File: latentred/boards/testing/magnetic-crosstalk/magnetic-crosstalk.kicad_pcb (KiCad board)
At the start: 4 copper layers, 82.4 x 89 mm, 93 parts, among them J1 STEWART_SS_74500_024, J2 SMA, J3 SMA, J4 SMA, J5 SMA, J6 SMA, J7 SMA, J8 SMA, J9 SMA

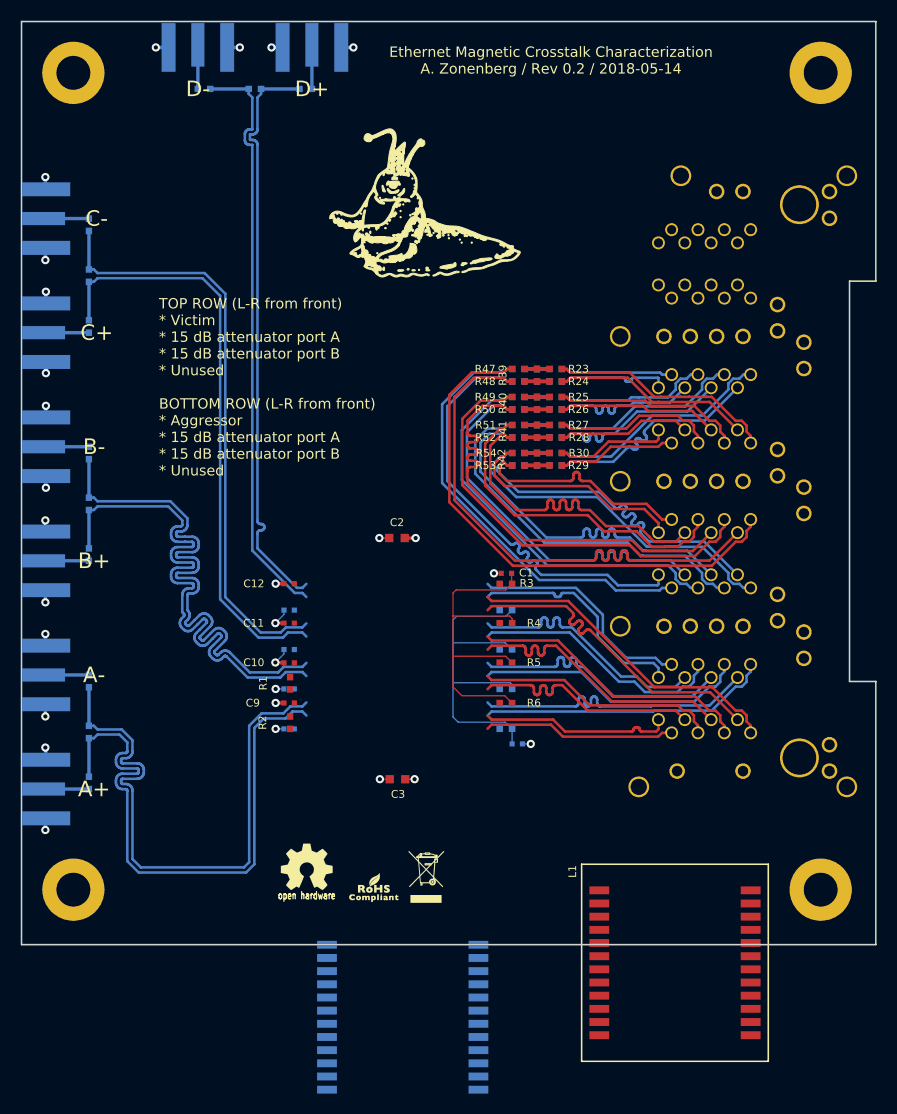
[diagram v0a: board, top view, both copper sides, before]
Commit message: Fixed pinout bugs. v0.2 PCB release.
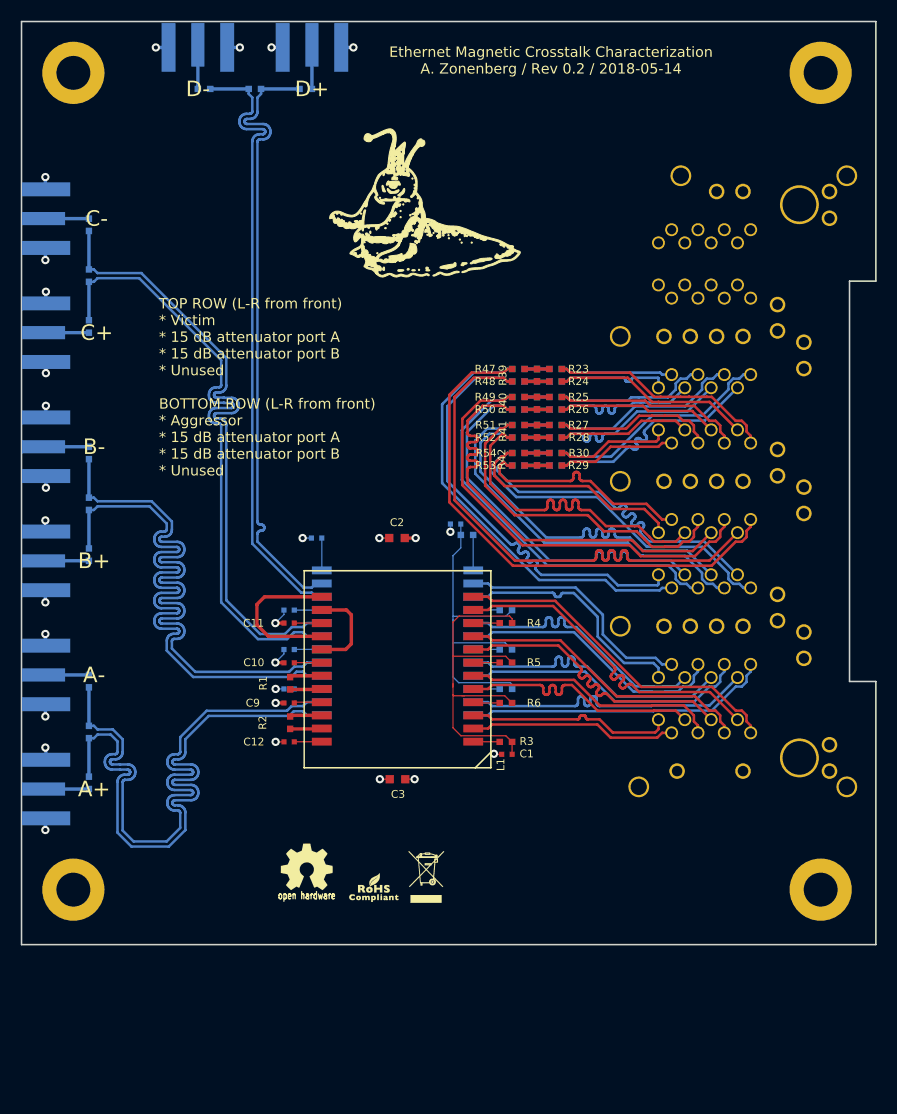
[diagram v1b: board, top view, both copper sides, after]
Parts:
- moved L1 38.9 mm to (201.2, 83.5), turned to 90 degrees
- moved L2 36.1 mm to (201.2, 80.9), turned to 270 degrees
- moved C8 22.0 mm to (206.8, 69.5), turned to 0 degrees
- moved R11 19.1 mm to (207.9, 70.5), turned to 0 degrees
- moved C7 18.6 mm to (193.4, 70.8)
- moved C1 17.5 mm to (211.8, 91.7)
- moved R3 15.3 mm to (211.7, 90.5)
- moved C12 15.3 mm to (190.8, 90.5)
- turned R10 to 180 degrees
- turned R7 to 270 degrees
- turned R8 to 270 degrees
- turned R9 to 270 degrees
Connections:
- L1 pad 11: /AGG_D_N -> /AGG_A_N
- L1 pad 12: /AGG_D_P -> /AGG_A_P
- L1 pad 15: Net-(C9-Pad2) -> Net-(C11-Pad2)
- L1 pad 16: Net-(L1-Pad16) -> Net-(L1-Pad13)
- L1 pad 17: Net-(L1-Pad17) -> Net-(L1-Pad14)
- L1 pad 2: /AGG_A_P -> /AGG_D_P
- L1 pad 21: Net-(C11-Pad2) -> Net-(C9-Pad2)
- L1 pad 22: Net-(L1-Pad19) -> Net-(L1-Pad22)
- L1 pad 23: Net-(L1-Pad20) -> Net-(L1-Pad23)
- L1 pad 3: /AGG_A_N -> /AGG_D_N
- L1 pad 5: /AGG_B_P -> /AGG_C_N
- L1 pad 6: /AGG_B_N -> /AGG_C_P
- L1 pad 8: /AGG_C_P -> /AGG_B_N
- L1 pad 9: /AGG_C_N -> /AGG_B_P
- L2 pad 11: /VIC_D_N -> /VIC_A_N
- L2 pad 12: /VIC_D_P -> /VIC_A_P
- L2 pad 13: /D_P -> /A_P
- L2 pad 14: /D_N -> /A_N
- L2 pad 15: Net-(C4-Pad2) -> Net-(C6-Pad2)
- L2 pad 16: /C_N -> /B_P
- L2 pad 17: /C_P -> /B_N
- L2 pad 19: /B_N -> /C_P
- L2 pad 2: /VIC_A_P -> /VIC_D_P
- L2 pad 20: /B_P -> /C_N
- L2 pad 21: Net-(C6-Pad2) -> Net-(C4-Pad2)
- L2 pad 22: /A_N -> /D_N
- L2 pad 23: /A_P -> /D_P
- L2 pad 3: /VIC_A_N -> /VIC_D_N
- L2 pad 5: /VIC_B_P -> /VIC_C_N
- L2 pad 6: /VIC_B_N -> /VIC_C_P
- L2 pad 8: /VIC_C_P -> /VIC_B_N
- L2 pad 9: /VIC_C_N -> /VIC_B_P
- R1 pad 1: Net-(L1-Pad17) -> Net-(L1-Pad19)
- R1 pad 2: Net-(L1-Pad16) -> Net-(L1-Pad20)
- R10 pad 1: /D_N -> /D_P
- R10 pad 2: /D_P -> /D_N
- R12 pad 2: Net-(L2-Pad4) -> Net-(L2-Pad10)
- R14 pad 2: Net-(L2-Pad10) -> Net-(L2-Pad4)
- R2 pad 1: Net-(L1-Pad14) -> Net-(L1-Pad22)
- R2 pad 2: Net-(L1-Pad13) -> Net-(L1-Pad23)
- R4 pad 2: Net-(L1-Pad4) -> Net-(L1-Pad10)
- R6 pad 2: Net-(L1-Pad10) -> Net-(L1-Pad4)
- R7 pad 1: /A_P -> /A_N
- R7 pad 2: /A_N -> /A_P
- R8 pad 1: /B_P -> /B_N
- R8 pad 2: /B_N -> /B_P
- R9 pad 1: /C_P -> /C_N
- R9 pad 2: /C_N -> /C_P
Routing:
- net Net-(L1-Pad13): track 0.00 -> 15.2 mm
- net Net-(L1-Pad14): track 0.00 -> 8.92 mm
- net /A_N: track 56.5 -> 60.3 mm
- net /A_P: track 56.5 -> 60.3 mm
- net /D_N: track 56.5 -> 60.3 mm
- net /D_P: track 56.5 -> 60.3 mm
- net /C_P: track 56.7 -> 60.4 mm
- net /C_N: track 56.7 -> 60.4 mm
- net /B_P: track 56.6 -> 60.3 mm
- net /B_N: track 56.6 -> 60.3 mm
- net Net-(L2-Pad1): track 0.00 -> 3.42 mm
- net Net-(L1-Pad19): track 0.00 -> 3.10 mm
- net Net-(L1-Pad22): track 0.00 -> 3.10 mm
- net Net-(C7-Pad2): track 0.02 -> 3.12 mm
- net Net-(L1-Pad20): track 0.00 -> 3.07 mm
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
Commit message: Updated magnetic-crosstalk to v0.3 respin
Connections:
- J1 pad A4: /AGG_B_N -> /AGG_C_P
- J1 pad A5: /AGG_C_P -> /AGG_C_N
- J1 pad A6: /AGG_C_N -> /AGG_B_N
- J1 pad B4: /VIC_B_N -> /VIC_C_P
- J1 pad B5: /VIC_C_P -> /VIC_C_N
- J1 pad B6: /VIC_C_N -> /VIC_B_N
- J1 pad C4: /A2_B_N -> /A2_C_P
- J1 pad C5: /A2_C_P -> /A2_C_N
- J1 pad C6: /A2_C_N -> /A2_B_N
- J1 pad D4: /A1X_B_N -> /A1X_C_P
- J1 pad D5: /A1X_C_P -> /A1X_C_N
- J1 pad D6: /A1X_C_N -> /A1X_B_N
- J1 pad E4: /A1_B_N -> /A1_C_P
- J1 pad E5: /A1_C_P -> /A1_C_N
- J1 pad E6: /A1_C_N -> /A1_B_N
- J1 pad F4: /A2X_B_N -> /A2X_C_P
- J1 pad F5: /A2X_C_P -> /A2X_C_N
- J1 pad F6: /A2X_C_N -> /A2X_B_N
- R27 pad 1: /A1Y_C_P -> /A1Y_D_N
- R27 pad 2: /A1_C_P -> /A1_D_N
- R28 pad 1: /A1Y_C_N -> /A1Y_D_P
- R28 pad 2: /A1_C_N -> /A1_D_P
- R29 pad 1: /A1Y_D_P -> /A1Y_C_P
- R29 pad 2: /A1_D_P -> /A1_C_P
- R30 pad 1: /A1Y_D_N -> /A1Y_C_N
- R30 pad 2: /A1_D_N -> /A1_C_N
- R31 pad 1: /A2Y_A_P -> /A2Y_A_N
- R31 pad 2: /A2_A_P -> /A2_A_N
- R32 pad 1: /A2Y_A_N -> /A2Y_A_P
- R32 pad 2: /A2_A_N -> /A2_A_P
- R33 pad 1: /A2Y_B_P -> /A2Y_B_N
- R33 pad 2: /A2_B_P -> /A2_B_N
- R34 pad 1: /A2Y_B_N -> /A2Y_B_P
- R34 pad 2: /A2_B_N -> /A2_B_P
- R35 pad 1: /A2Y_C_P -> /A2Y_D_P
- R35 pad 2: /A2_C_P -> /A2_D_P
- R36 pad 1: /A2Y_C_N -> /A2Y_D_N
- R36 pad 2: /A2_C_N -> /A2_D_N
- R37 pad 1: /A2Y_D_P -> /A2Y_C_P
- R37 pad 2: /A2_D_P -> /A2_C_P
- R38 pad 1: /A2Y_D_N -> /A2Y_C_N
- R38 pad 2: /A2_D_N -> /A2_C_N
- R41 pad 1: /A1Y_C_N -> /A1Y_D_P
- R41 pad 2: /A1Y_C_P -> /A1Y_D_N
- R42 pad 1: /A1Y_D_N -> /A1Y_C_N
- R42 pad 2: /A1Y_D_P -> /A1Y_C_P
- R43 pad 1: /A2Y_A_N -> /A2Y_A_P
- R43 pad 2: /A2Y_A_P -> /A2Y_A_N
- R44 pad 1: /A2Y_B_N -> /A2Y_B_P
- R44 pad 2: /A2Y_B_P -> /A2Y_B_N
- R45 pad 1: /A2Y_C_N -> /A2Y_D_N
- R45 pad 2: /A2Y_C_P -> /A2Y_D_P
- R46 pad 1: /A2Y_D_N -> /A2Y_C_N
- R46 pad 2: /A2Y_D_P -> /A2Y_C_P
- R51 pad 1: /A1X_C_P -> /A1X_D_N
- R51 pad 2: /A1Y_C_P -> /A1Y_D_N
- R52 pad 1: /A1X_C_N -> /A1X_D_P
- R52 pad 2: /A1Y_C_N -> /A1Y_D_P
- R53 pad 1: /A1X_D_P -> /A1X_C_P
- R53 pad 2: /A1Y_D_P -> /A1Y_C_P
- R54 pad 1: /A1X_D_N -> /A1X_C_N
- R54 pad 2: /A1Y_D_N -> /A1Y_C_N
- R55 pad 1: /A2X_A_P -> /A2X_A_N
- R55 pad 2: /A2Y_A_P -> /A2Y_A_N
- R56 pad 1: /A2X_A_N -> /A2X_A_P
- R56 pad 2: /A2Y_A_N -> /A2Y_A_P
- R57 pad 1: /A2X_B_P -> /A2X_B_N
- R57 pad 2: /A2Y_B_P -> /A2Y_B_N
- R58 pad 1: /A2X_B_N -> /A2X_B_P
- R58 pad 2: /A2Y_B_N -> /A2Y_B_P
- R59 pad 1: /A2X_C_P -> /A2X_D_P
- R59 pad 2: /A2Y_C_P -> /A2Y_D_P
- R60 pad 1: /A2X_C_N -> /A2X_D_N
- R60 pad 2: /A2Y_C_N -> /A2Y_D_N
- R61 pad 1: /A2X_D_P -> /A2X_C_P
- R61 pad 2: /A2Y_D_P -> /A2Y_C_P
- R62 pad 1: /A2X_D_N -> /A2X_C_N
- R62 pad 2: /A2Y_D_N -> /A2Y_C_N
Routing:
- net /A2_C_P: track 38.4 -> 47.2 mm
- net /A2_C_N: track 38.4 -> 47.2 mm
- net /A1X_C_P: track 32.2 -> 23.9 mm
- net /A1X_C_N: track 32.2 -> 23.9 mm
- net /A2_D_N: track 42.3 -> 34.8 mm
- net /A2_D_P: track 42.3 -> 34.9 mm
- net /AGG_C_P: track 24.7 -> 29.6 mm
- net /AGG_C_N: track 24.7 -> 29.6 mm
- net /A1X_D_P: track 21.9 -> 26.2 mm
- net /A1X_D_N: track 21.9 -> 26.2 mm
- net /A2_A_P: track 33.1 -> 29.4 mm
- net /A2_A_N: track 33.1 -> 29.5 mm
- net /A1_C_N: track 12.9 -> 16.6 mm
- net /A2_B_N: track 36.3 -> 33.3 mm
- net /A2_B_P: track 36.3 -> 33.3 mm
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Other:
- board text added: "Ethernet Magnetic Crosstalk Characterization A. Zonenberg / Rev 0.3 / 2018-05-15"
- board text removed: "Ethernet Magnetic Crosstalk Characterization A. Zonenberg / Rev 0.2 / 2018-05-14"
